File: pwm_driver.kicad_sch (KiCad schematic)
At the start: 6 parts, among them U5 PCA9685PW, U6 PCA9685PW

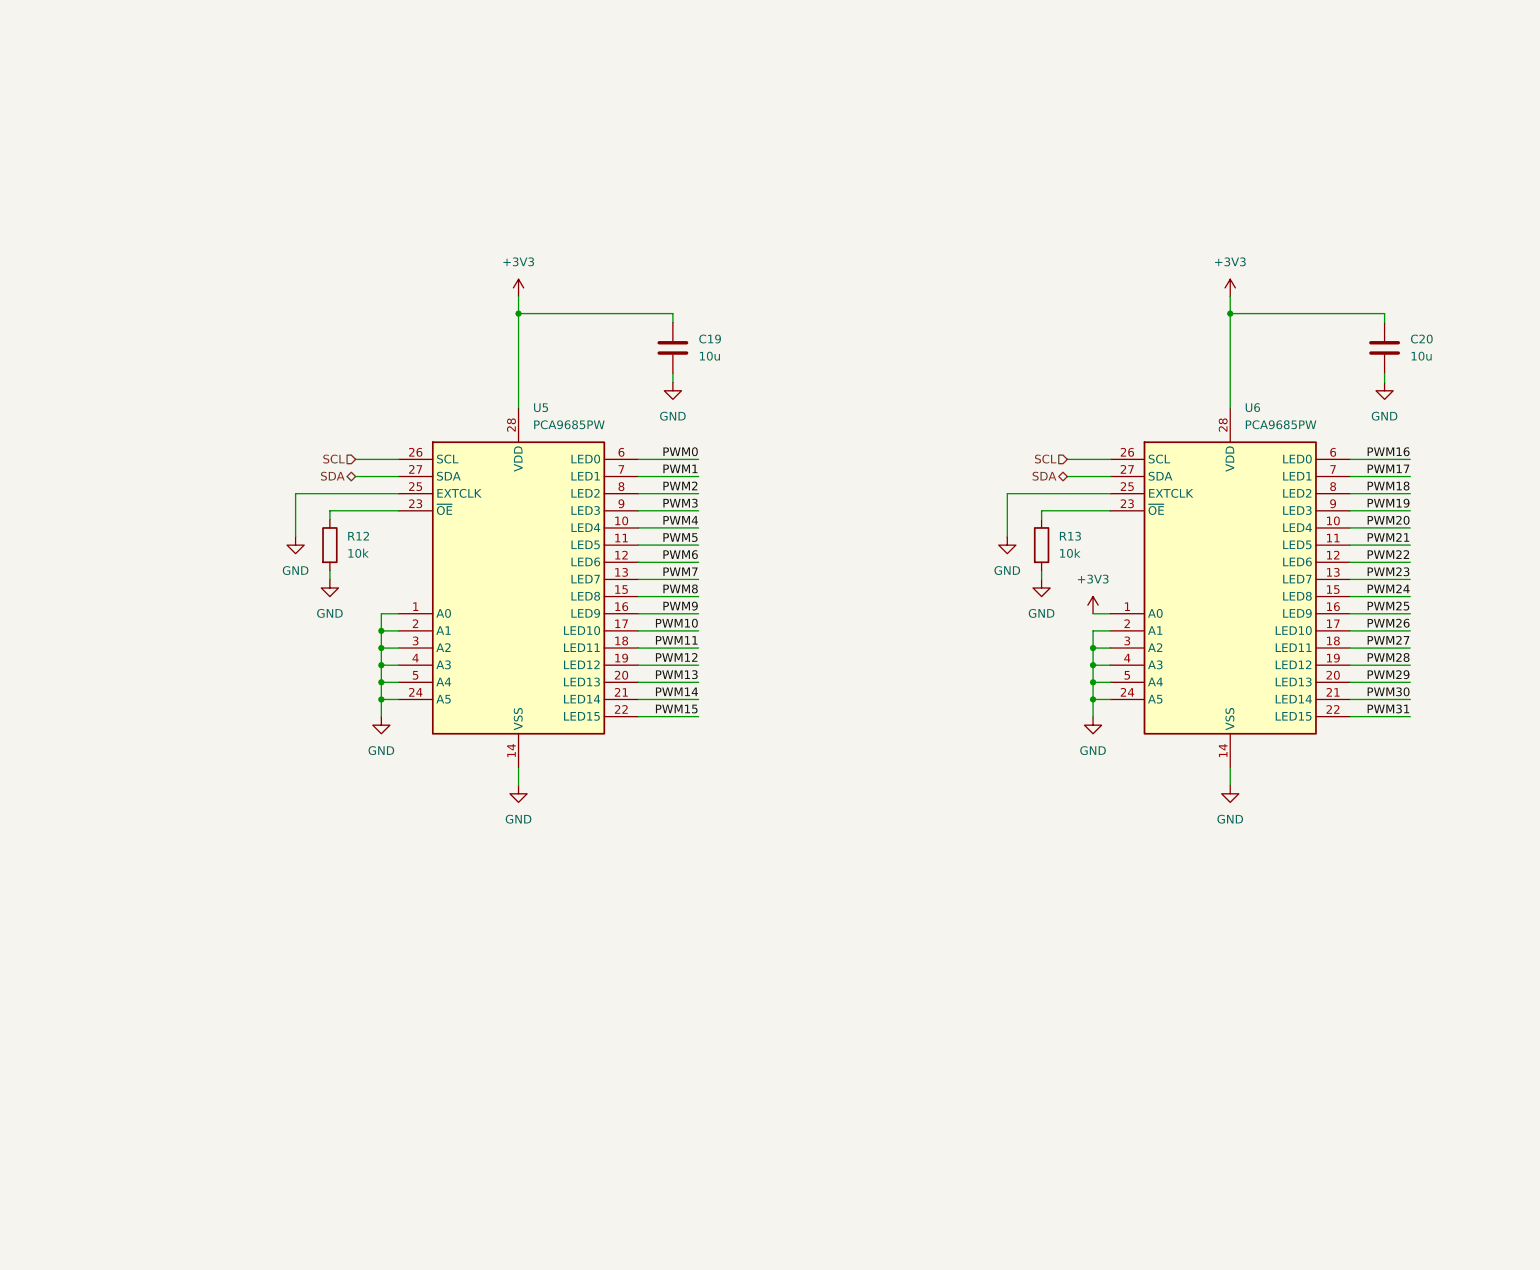
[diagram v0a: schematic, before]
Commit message: Add servo connectors
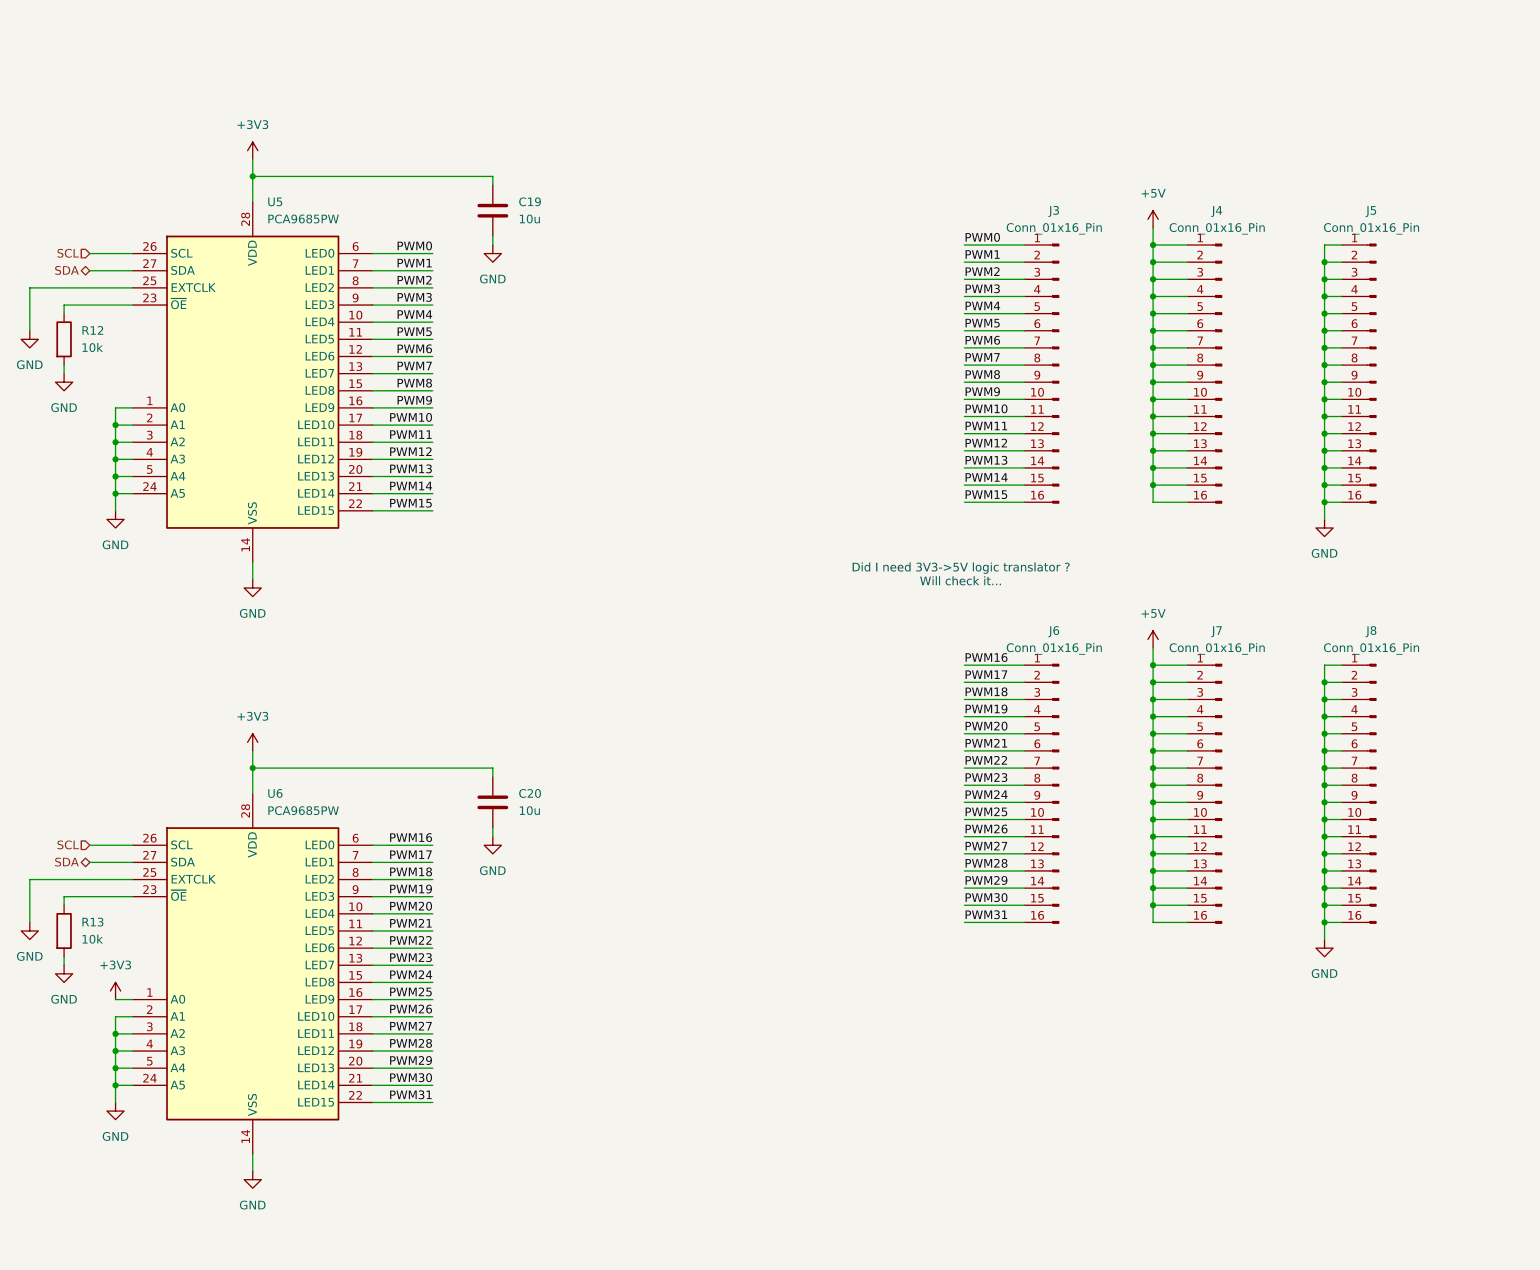
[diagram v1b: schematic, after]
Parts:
- added J3, J4, J5, J6, J7, J8: Conn_01x16_Pin, symbol Connector:Conn_01x16_Pin
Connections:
- net GND: now also J5.1 (Pin_1), J5.10 (Pin_10), J5.11 (Pin_11), J5.12 (Pin_12), J5.13 (Pin_13), J5.14 (Pin_14), J5.15 (Pin_15), J5.16 (Pin_16), J5.2 (Pin_2), J5.3 (Pin_3), J5.4 (Pin_4), J5.5 (Pin_5), J5.6 (Pin_6), J5.7 (Pin_7), J5.8 (Pin_8), J5.9 (Pin_9), J8.1 (Pin_1), J8.10 (Pin_10), J8.11 (Pin_11), J8.12 (Pin_12), J8.13 (Pin_13), J8.14 (Pin_14), J8.15 (Pin_15), J8.16 (Pin_16), J8.2 (Pin_2), J8.3 (Pin_3), J8.4 (Pin_4), J8.5 (Pin_5), J8.6 (Pin_6), J8.7 (Pin_7), J8.8 (Pin_8), J8.9 (Pin_9)
- net PWM0: now also J3.1 (Pin_1)
- net PWM1: now also J3.2 (Pin_2)
- net PWM10: now also J3.11 (Pin_11)
- net PWM11: now also J3.12 (Pin_12)
- net PWM12: now also J3.13 (Pin_13)
- net PWM13: now also J3.14 (Pin_14)
- net PWM14: now also J3.15 (Pin_15)
- net PWM15: now also J3.16 (Pin_16)
- net PWM16: now also J6.1 (Pin_1)
- net PWM17: now also J6.2 (Pin_2)
- net PWM18: now also J6.3 (Pin_3)
- net PWM19: now also J6.4 (Pin_4)
- net PWM2: now also J3.3 (Pin_3)
- net PWM20: now also J6.5 (Pin_5)
- net PWM21: now also J6.6 (Pin_6)
- net PWM22: now also J6.7 (Pin_7)
- net PWM23: now also J6.8 (Pin_8)
- net PWM24: now also J6.9 (Pin_9)
- net PWM25: now also J6.10 (Pin_10)
- net PWM26: now also J6.11 (Pin_11)
- net PWM27: now also J6.12 (Pin_12)
- net PWM28: now also J6.13 (Pin_13)
- net PWM29: now also J6.14 (Pin_14)
- net PWM3: now also J3.4 (Pin_4)
- net PWM30: now also J6.15 (Pin_15)
- net PWM31: now also J6.16 (Pin_16)
- net PWM4: now also J3.5 (Pin_5)
- net PWM5: now also J3.6 (Pin_6)
- net PWM6: now also J3.7 (Pin_7)
- net PWM7: now also J3.8 (Pin_8)
- net PWM8: now also J3.9 (Pin_9)
- net PWM9: now also J3.10 (Pin_10)
- new net +5V: J4.1 (Pin_1), J4.10 (Pin_10), J4.11 (Pin_11), J4.12 (Pin_12), J4.13 (Pin_13), J4.14 (Pin_14), J4.15 (Pin_15), J4.16 (Pin_16), J4.2 (Pin_2), J4.3 (Pin_3), J4.4 (Pin_4), J4.5 (Pin_5), J4.6 (Pin_6), J4.7 (Pin_7), J4.8 (Pin_8), J4.9 (Pin_9), J7.1 (Pin_1), J7.10 (Pin_10), J7.11 (Pin_11), J7.12 (Pin_12), J7.13 (Pin_13), J7.14 (Pin_14), J7.15 (Pin_15), J7.16 (Pin_16), J7.2 (Pin_2), J7.3 (Pin_3), J7.4 (Pin_4), J7.5 (Pin_5), J7.6 (Pin_6), J7.7 (Pin_7), J7.8 (Pin_8), J7.9 (Pin_9)
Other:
- note added: "Did I need 3V3->5V logic translator ? Will check it..."
- moved on the sheet: C19, C20, R12, R13, U5, U6

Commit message: Update schematic
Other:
- note added: "Did I need 3V3->5V logic translator ? Have to check it..."
- note added: "PWM Drivers"
- note added: "Servo Connectors"
- note removed: "Did I need 3V3->5V logic translator ? Will check it..."
- moved on the sheet: C19, J3, J4, J5, J6, J7, J8, R12, U5
